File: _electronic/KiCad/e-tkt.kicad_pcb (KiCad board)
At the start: 2 copper layers, 99.6 x 76.2 mm, 97 parts, among them J1 USB4105-GF-A, Q1 SS8050-G, Q2 SS8050-G, U1 USB6B1, U2 AZ1117I-3.3, U3 FT231XS, U4 ESP32-WROOM-32

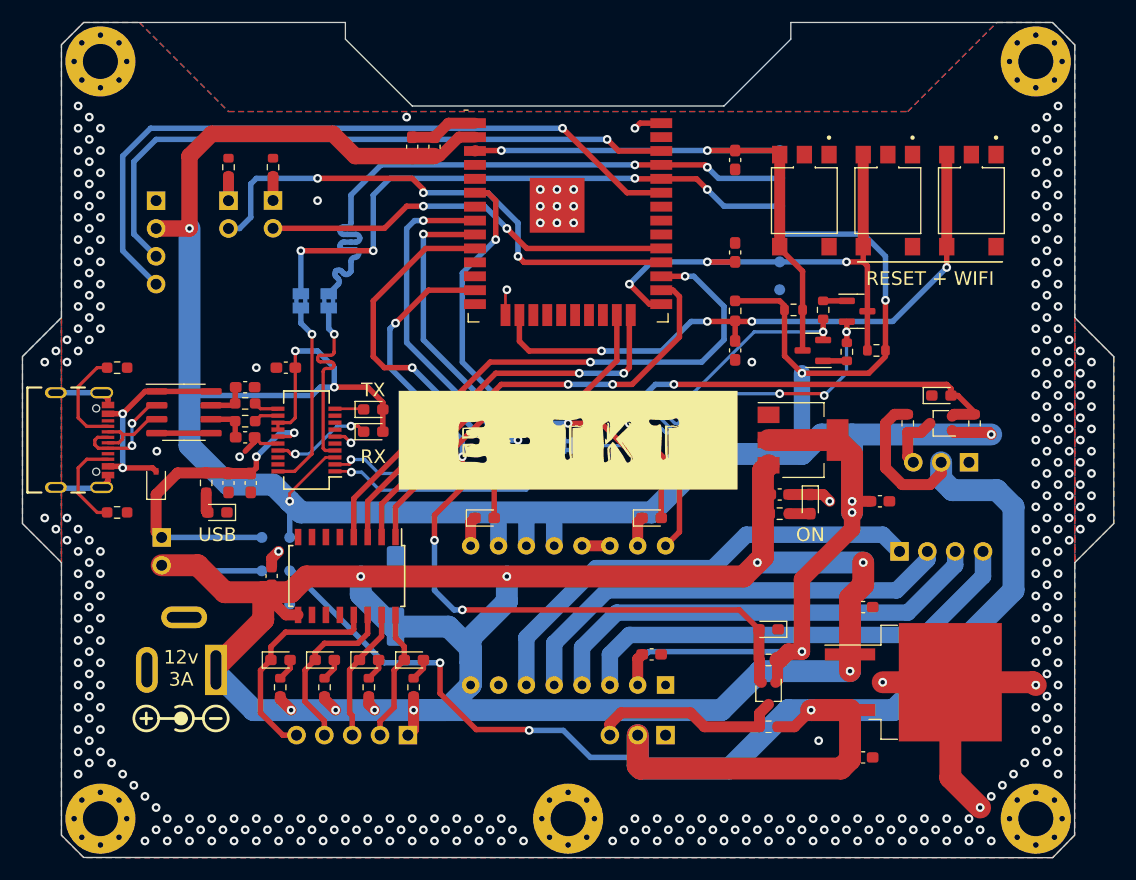
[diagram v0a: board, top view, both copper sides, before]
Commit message: led resistors, better pcb layout, omron tact
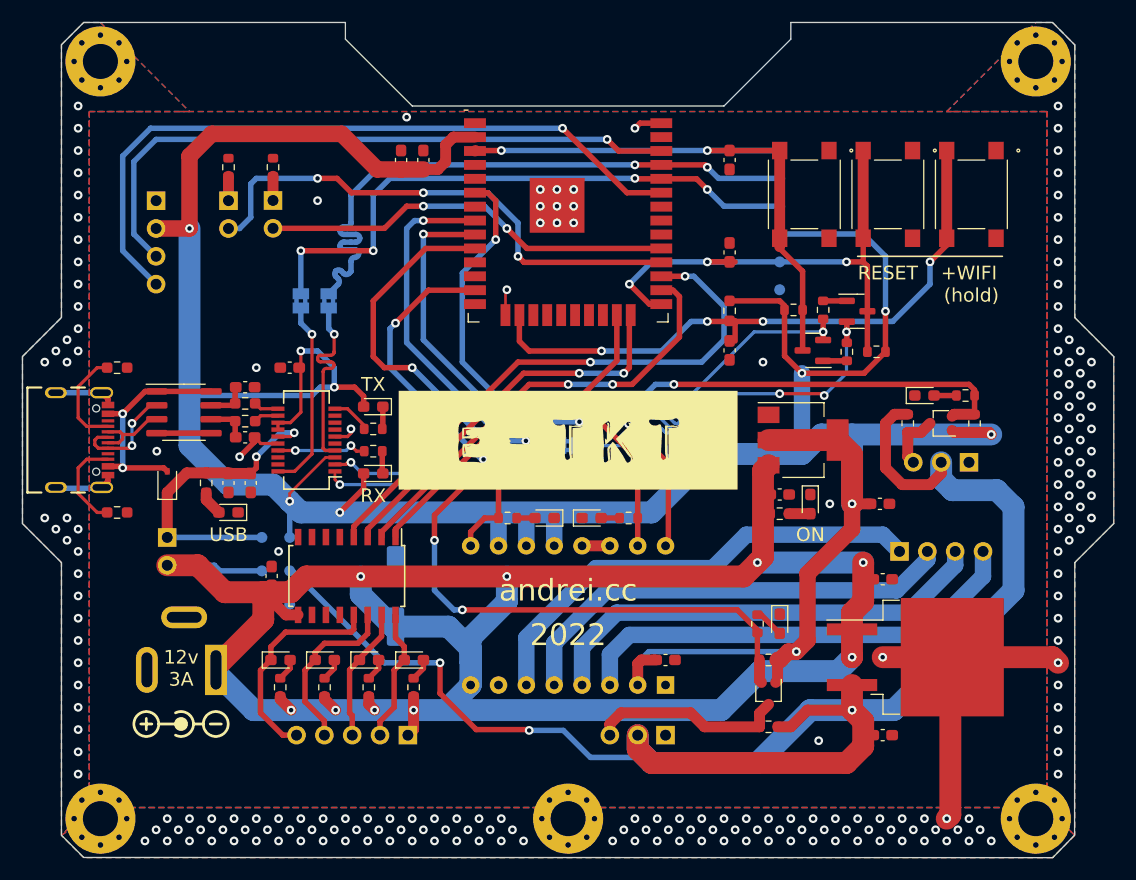
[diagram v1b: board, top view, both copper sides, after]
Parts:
- removed S_BOOT1, S_RESET1, S_WIFIRESET1: TS06-667-25-BK-100-G-SMT-TR, SnapEDA Library:SW_TS06-667-25-BK-100-G-SMT-TR
- added R22: 47R, Resistor_SMD:R_0603_1608Metric, F.Cu at (160.5, -188.5)
- added R23: 47R, Resistor_SMD:R_0603_1608Metric, F.Cu at (160.5, -190.5)
- added R24: 47R, Resistor_SMD:R_0603_1608Metric, F.Cu at (214.6, -193.5)
- added R25: 47R, Resistor_SMD:R_0603_1608Metric, F.Cu at (195.6, -172.7)
- added R26: 47R, Resistor_SMD:R_0603_1608Metric, F.Cu at (172.8, -182.4)
- added R27: 47R, Resistor_SMD:R_0603_1608Metric, F.Cu at (183.8, -182.4)
- added SW1: B3FS-1000, b3fs:B3FS-1000, F.Cu at (207.5, -211.9)
- added SW2: B3FS-1000, b3fs:B3FS-1000, F.Cu at (199.9, -211.9)
- added SW3: B3FS-1000, b3fs:B3FS-1000, F.Cu at (215.1, -211.9)
- R20, R21: value 0R -> 47R
- moved D4 5.48 mm to (176.2, -182.4), turned to 180 degrees
- moved D1 5.47 mm to (180.5, -182.4)
- moved D_RX1 3.81 mm to (160.5, -186.4), turned to 180 degrees
- moved C14 3.10 mm to (207.0, -176.8)
- moved C17 2.70 mm to (207.0, -162.6)
- moved U_6v2 2.29 mm to (210.0, -169.7)
- moved C7 1.59 mm to (165.1, -215.0)
- moved C6 1.59 mm to (163.1, -215.0)
- moved D9 1.55 mm to (210.8, -193.5)
- moved C9 1.37 mm to (187.2, -169.4)
- moved D10 1.14 mm to (197.6, -172.7), turned to -90 degrees
- moved D2 1.02 mm to (141.7, -185.6)
- moved D_USBIN1 1.02 mm to (147.3, -182.9)
- moved C1 0.51 mm to (193.0, -197.7)
- moved C3 0.51 mm to (193.0, -206.6)
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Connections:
- A_DRIVER1 pad 15: Net-(A_DRIVER1-Pad15) -> IO32 NEMA STEP
- A_DRIVER1 pad 9: Net-(A_DRIVER1-Pad9) -> IO25 NEMA ENA
- D1 pad 1: Net-(A_DRIVER1-Pad15) -> GNDREF
- D1 pad 2: IO32 NEMA STEP -> Net-(D1-Pad2)
- D10 pad 2: IO14 SERVO -> Net-(D10-Pad2)
- D4 pad 1: Net-(A_DRIVER1-Pad9) -> GNDREF
- D4 pad 2: IO25 NEMA ENA -> Net-(D4-Pad2)
- D9 pad 2: IO34 HALL -> Net-(D9-Pad2)
- D_RX1 pad 1: Net-(D_RX1-Pad1) -> Net-(R22-Pad1)
- D_TX1 pad 1: Net-(D_TX1-Pad1) -> Net-(R23-Pad1)
- U3 pad 10: Net-(D_TX1-Pad1) -> Net-(R23-Pad2)
- U3 pad 17: Net-(D_RX1-Pad1) -> Net-(U3-Pad17)
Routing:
- net Net-(D_RX1-Pad1): track 9.22 -> 0.00 mm, vias 2 -> 0
- net Net-(U3-Pad17): track 0.00 -> 8.27 mm, vias 0 -> 2
- net GNDREF: track 65.2 -> 58.8 mm, vias 325 -> 214
- net IO25 NEMA ENA: track 40.7 -> 45.9 mm
- net +12V: track 212.9 -> 208.3 mm
- net Net-(R23-Pad2): track 0.00 -> 3.62 mm
- net Net-(D10-Pad2): track 0.00 -> 2.74 mm
- net Net-(A_DRIVER1-Pad15): track 2.70 -> 0.00 mm
- net Net-(A_DRIVER1-Pad9): track 2.70 -> 0.00 mm
- net Net-(D_TX1-Pad1): track 2.62 -> 0.00 mm
- net Net-(R23-Pad1): track 0.00 -> 2.05 mm
- net Net-(R22-Pad1): track 0.00 -> 2.05 mm
- net Net-(D9-Pad2): track 0.00 -> 2.05 mm
- net +3.3V: track 302.7 -> 304.6 mm
- net Net-(D4-Pad2): track 0.00 -> 1.68 mm
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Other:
- board text added: "(hold)"
- board text added: "+WIFI"
- board text added: "2022"
- board text added: "RESET"
- board text added: "andrei.cc"
- board text removed: "RESET + WIFI"

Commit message: rev1 schematics export
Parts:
- renumbered U_6v2 to U5, U_DRIVER1 to U6
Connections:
- net /D1+ renamed /USBD1+
- net /D1- renamed /USBD1-

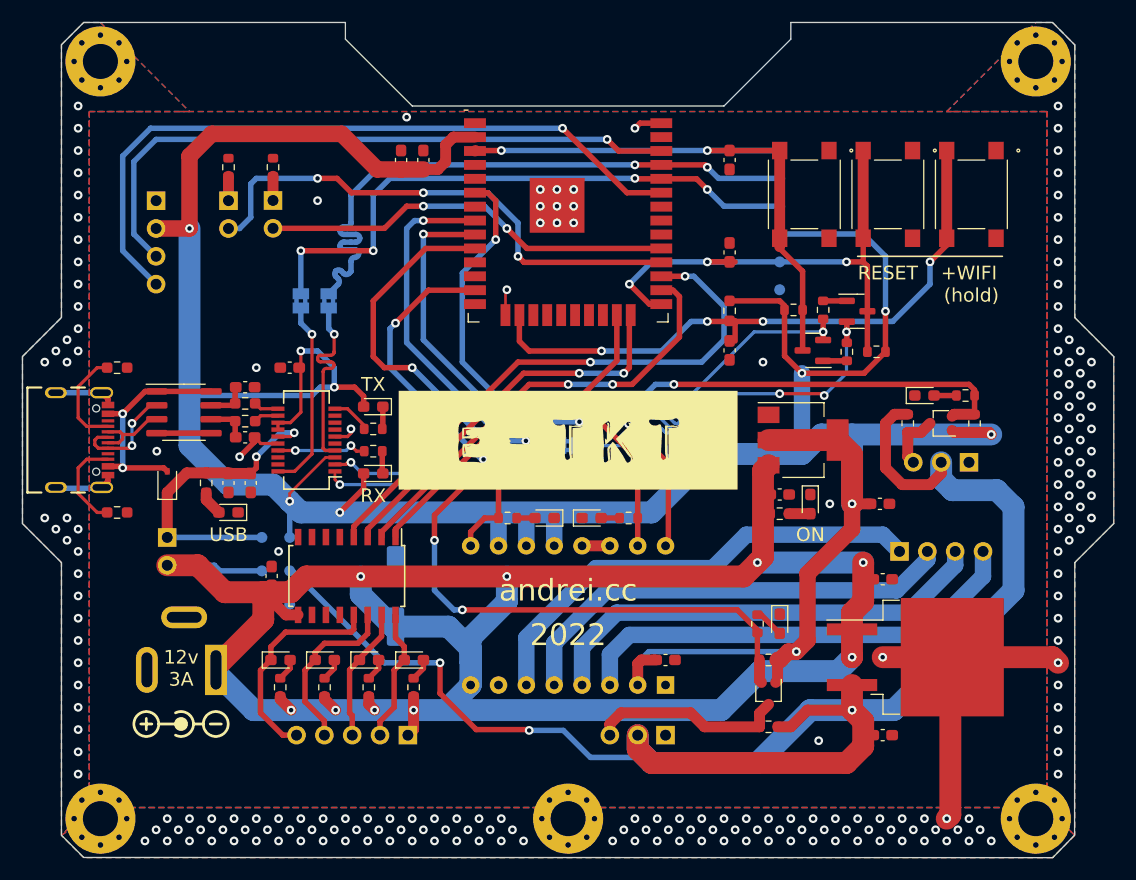
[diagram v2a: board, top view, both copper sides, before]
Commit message: ftdi revision, removed usb vcc jumper
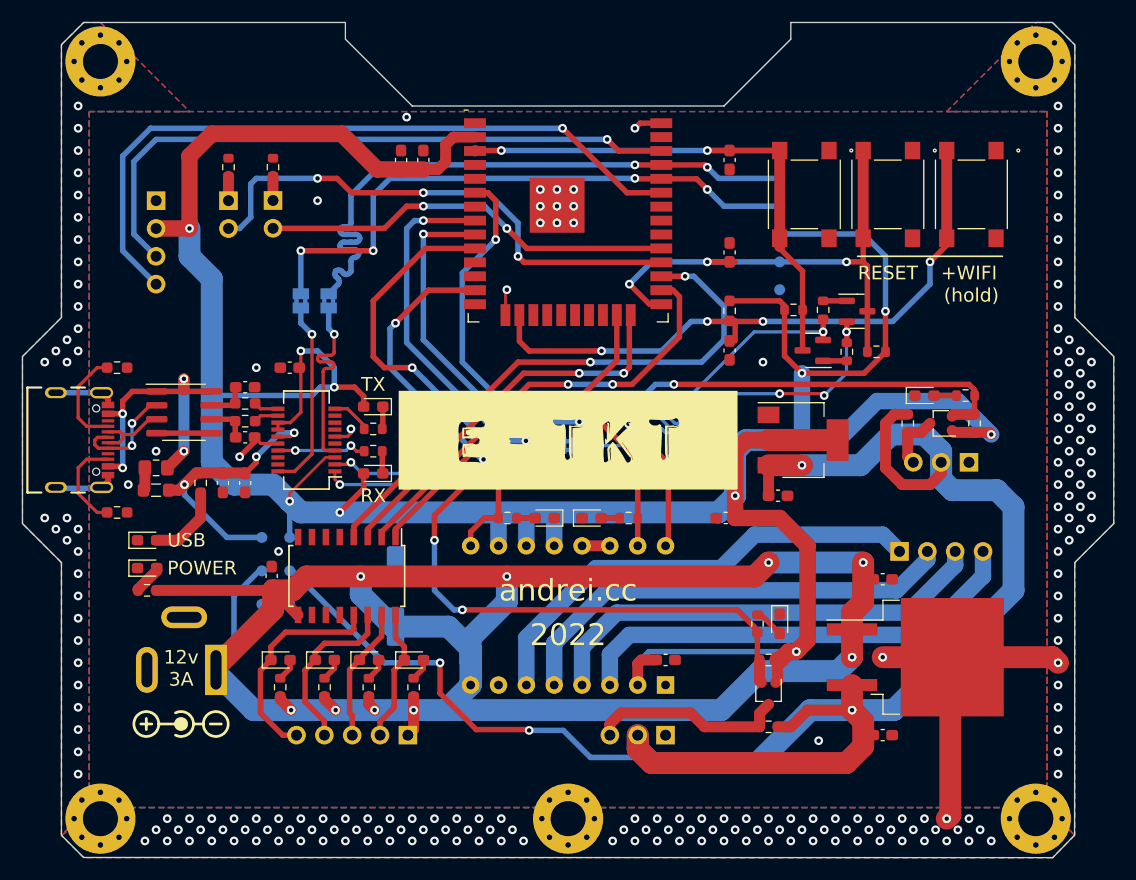
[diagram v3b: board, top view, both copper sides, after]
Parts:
- removed D2: BAT760,115, Diode_SMD:D_SOD-323
- removed J_USBPOWER1: Conn_01x02_Male, Connector_PinHeader_2.54mm:PinHeader_1x02_P2.54mm_Vertical
- added F1: 6V 40A 750mA, Fuse:Fuse_0805_2012Metric_Pad1.15x1.40mm_HandSolder, F.Cu at (140.7, -186.9)
- added FB1: 6V 750mA, Inductor_SMD:L_0805_2012Metric_Pad1.05x1.20mm_HandSolder, F.Cu at (140.7, -184.9)
- moved D11 60.8 mm to (139.9, -177.8), turned to 0 degrees
- moved R2 58.1 mm to (139.9, -175.8), turned to 180 degrees
- moved C11 14.1 mm to (192.7, -182.4), turned to 180 degrees
- moved D_USBIN1 7.84 mm to (139.9, -180.3), turned to 0 degrees
- moved C15 0.51 mm to (148.8, -185.6)
- moved R6 0.51 mm to (144.8, -185.6)
- moved C2 0.51 mm to (146.8, -185.6)
- moved C10 0.19 mm to (197.5, -184.4)
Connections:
- net +5V renamed VBUS
- C10 pad 1: +12V -> +6V
- U2 pad 3: +12V -> +6V
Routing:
- net +6V: track 150.1 -> 171.5 mm, vias 3 -> 4
- net +12V: track 208.3 -> 201.7 mm
- net Net-(F1-Pad1): track 20.8 -> 27.0 mm, vias 2 -> 4
- net Net-(D_USBIN1-Pad2): track 2.26 -> 7.14 mm
- net VBUS: track 28.8 -> 25.2 mm, vias 2 -> 3
- net Net-(F1-Pad2): track 0.00 -> 2.08 mm
- net +3.3V: track 304.6 -> 303.5 mm
- net Net-(D11-Pad2): track 1.97 -> 2.74 mm
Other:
- board text added: "5v (USB)"
- board text added: "POWER"
- board text removed: "5v"
- board text removed: "ON"
- board text removed: "USB MODE"
